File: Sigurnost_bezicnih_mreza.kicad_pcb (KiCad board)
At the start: 2 copper layers, 85.6 x 62 mm, 6 parts, among them J1 SIM_Card, J2 Conn_01x06_Male

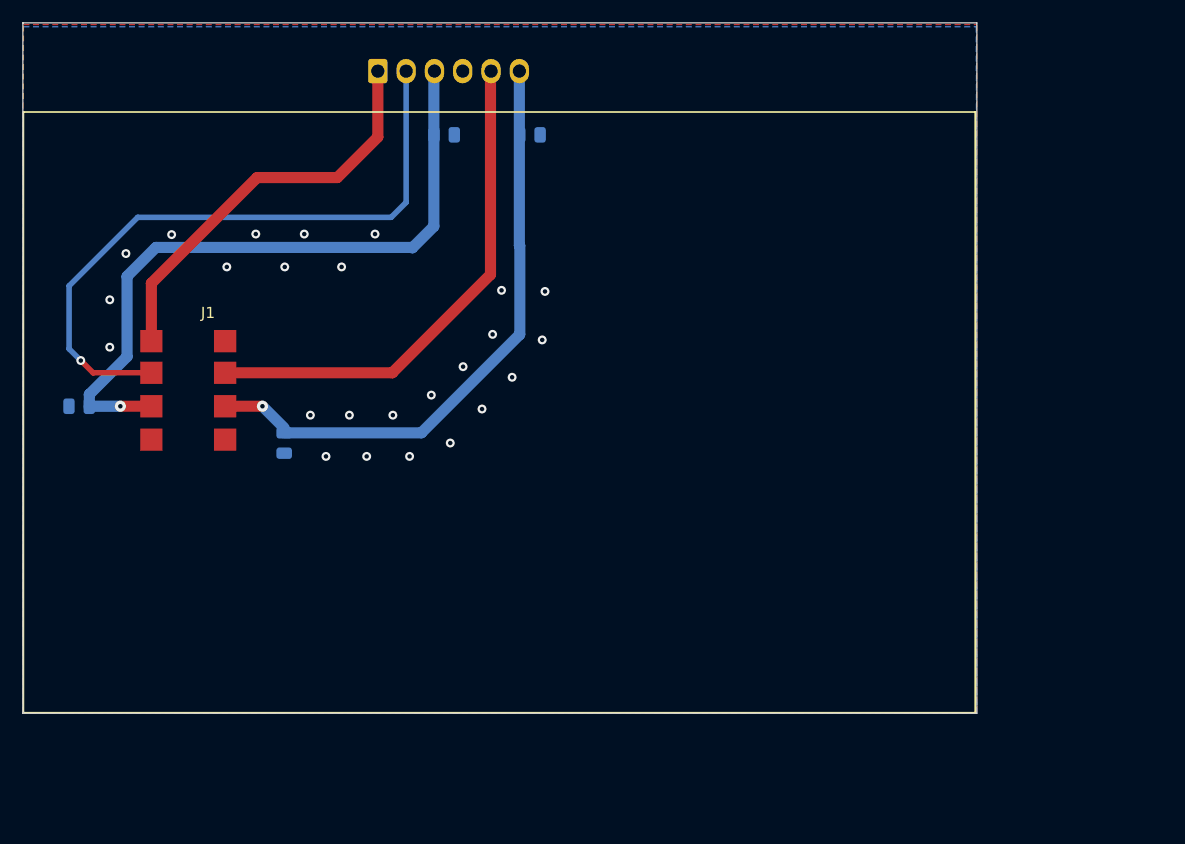
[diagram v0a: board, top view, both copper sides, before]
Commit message: dimensions adjusted
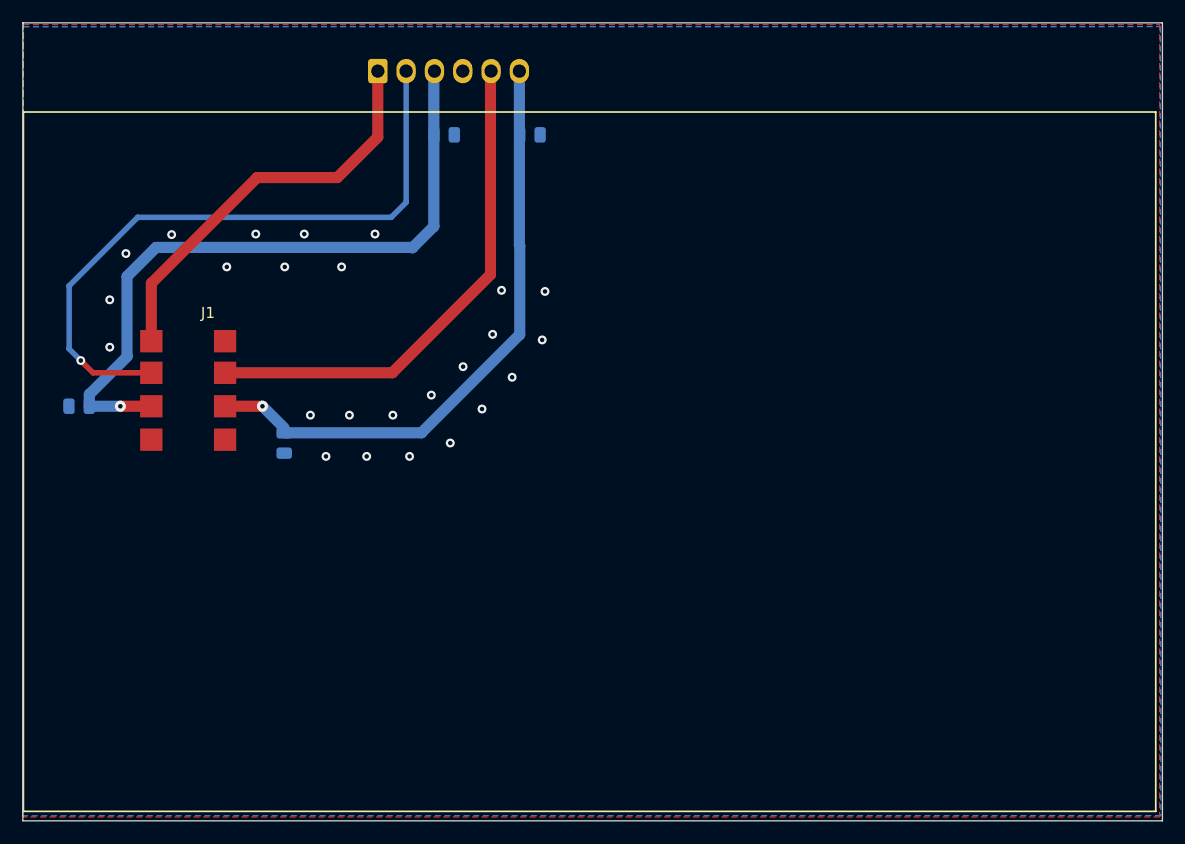
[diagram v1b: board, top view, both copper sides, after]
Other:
- board size 85.6 x 62 mm -> 102.2 x 71.6 mm
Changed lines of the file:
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@@
     )
   )
-  (gr_rect (start 89.45 142.35) (end 174.85 88.45) (layer "F.SilkS") (width 0.15) (fill none))
-  (gr_rect (start 89.4 80.45) (end 175 142.4) (layer "Edge.Cuts") (width 0.1) (fill none))
+  (gr_rect (start 89.45 151.2) (end 191.05 88.45) (layer "F.SilkS") (width 0.15) (fill none))
+  (gr_rect (start 89.4 80.45) (end 191.65 152.05) (layer "Edge.Cuts") (width 0.1) (fill none))
   (segment (start 117.62 94.33) (end 121.25 90.7) (width 1) (layer "F.Cu") (net 1))
   (segment (start 121.25 90.7) (end 121.25 84.78) (width 1) (layer "F.Cu") (net 1))
@@
     (polygon
       (pts
-        (xy 175 142.4)
-        (xy 89.4 142.4)
+        (xy 191.4 151.7)
+        (xy 89.4 151.7)
         (xy 89.45 80.6)
-        (xy 175 80.6)
+        (xy 191.4 80.6)
       )
     )
@@
     (polygon
       (pts
-        (xy 175 142.4)
-        (xy 89.4 142.4)
+        (xy 191.510214 151.587054)
+        (xy 89.400919 151.600039)
         (xy 89.45 80.8)
-        (xy 174.95 80.8)
+        (xy 191.459295 80.787015)
       )
     )
